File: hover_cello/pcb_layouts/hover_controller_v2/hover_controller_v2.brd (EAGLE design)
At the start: 101.6 x 50.8 mm, 33 parts, among them IC1 74LS279N, U1 L298

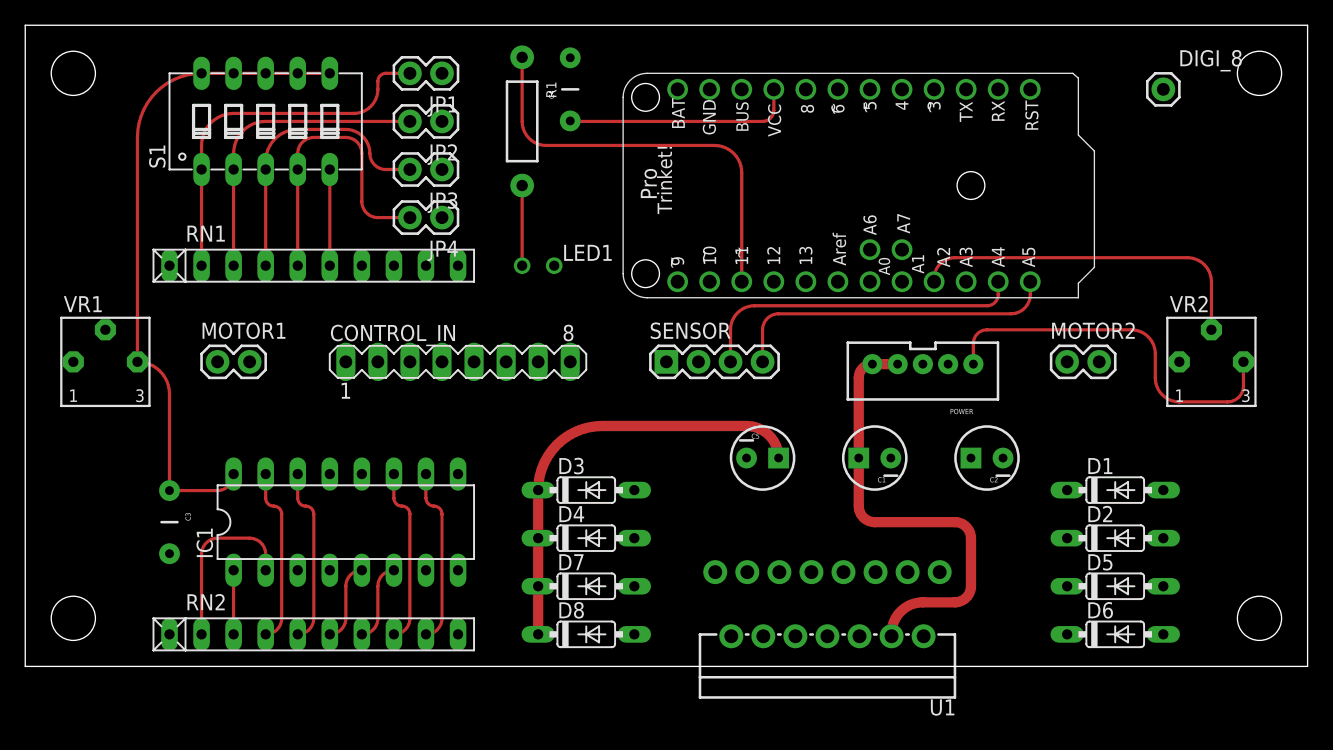
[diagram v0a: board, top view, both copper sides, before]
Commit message: wrote and tested V1.0 firmware for hover cello
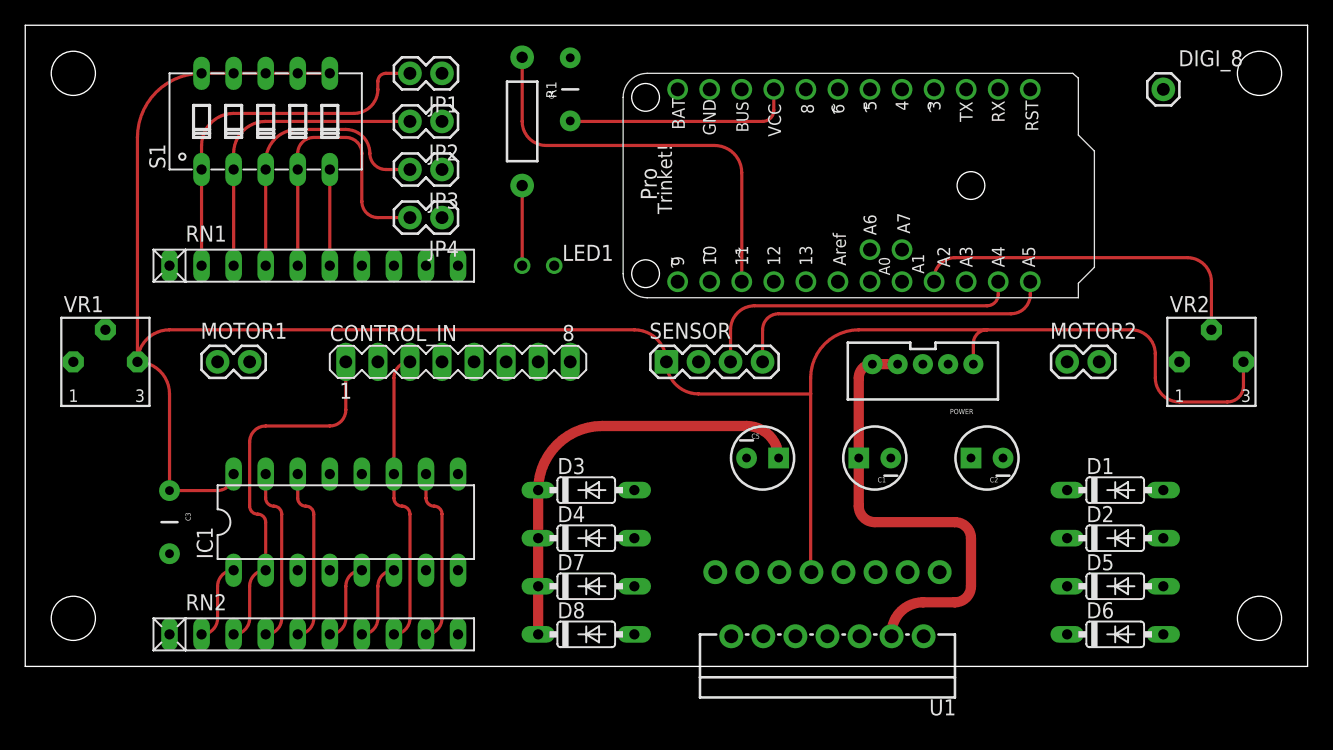
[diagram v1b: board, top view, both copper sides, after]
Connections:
- net R1: now also RN2.2; no longer RN2.3
- net S1: now also RN2.3; no longer RN2.2
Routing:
- net VCC: track 81.4 -> 168.9 mm
- net S1: track 13.8 -> 29.3 mm
- net S2: track 13.8 -> 23.2 mm
- net R1: track 5.08 -> 6.13 mm
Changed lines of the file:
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@@
 <contactref element="VR1" pad="3"/>
 <contactref element="VR2" pad="3"/>
-<wire x1="75.12" y1="23.95" x2="75.12" y2="25.59" width="0.254" layer="1"/>
-<wire x1="75.12" y1="25.59" x2="76.2" y2="26.67" width="0.254" layer="1" curve="-90"/>
+<wire x1="76.2" y1="26.67" x2="75.12" y2="25.59" width="0.254" layer="1" curve="90"/>
 <wire x1="87.63" y1="26.67" x2="89.535" y2="24.765" width="0.254" layer="1" curve="-90"/>
 <wire x1="89.535" y1="24.765" x2="89.535" y2="22.86" width="0.254" layer="1"/>
@@
 <wire x1="13.97" y1="46.99" x2="8.89" y2="41.91" width="0.254" layer="1" curve="90"/>
 <wire x1="8.89" y1="41.91" x2="8.89" y2="24.13" width="0.254" layer="1"/>
-<wire x1="74.93" y1="16.51" x2="75.12" y2="23.95" width="0" layer="19" extent="1-1"/>
-<wire x1="62.29" y1="7.47" x2="74.93" y2="16.51" width="0" layer="19" extent="1-1"/>
-<wire x1="50.8" y1="24.13" x2="62.29" y2="7.47" width="0" layer="19" extent="1-1"/>
-<wire x1="24.13" y1="46.99" x2="50.8" y2="24.13" width="0" layer="19" extent="1-1"/>
+<wire x1="75.12" y1="23.95" x2="75.12" y2="25.59" width="0.254" layer="1"/>
+<wire x1="62.29" y1="7.47" x2="62.23" y2="7.53" width="0.254" layer="1" curve="-90"/>
+<wire x1="62.23" y1="21.59" x2="62.23" y2="7.53" width="0.254" layer="1"/>
+<wire x1="62.23" y1="21.59" x2="62.23" y2="22.86" width="0.254" layer="1"/>
+<wire x1="62.23" y1="22.86" x2="66.04" y2="26.67" width="0.254" layer="1" curve="-90"/>
+<wire x1="66.04" y1="26.67" x2="76.2" y2="26.67" width="0.254" layer="1"/>
+<wire x1="53.34" y1="21.59" x2="50.8" y2="24.13" width="0.254" layer="1" curve="-90"/>
+<wire x1="53.34" y1="21.59" x2="62.23" y2="21.59" width="0.254" layer="1"/>
+<wire x1="50.8" y1="24.13" x2="48.26" y2="26.67" width="0.254" layer="1" curve="90"/>
+<wire x1="11.43" y1="26.67" x2="8.89" y2="24.13" width="0.254" layer="1" curve="90"/>
+<wire x1="48.26" y1="26.67" x2="11.43" y2="26.67" width="0.254" layer="1"/>
+<wire x1="75.12" y1="23.95" x2="74.93" y2="16.51" width="0" layer="19" extent="1-1"/>
 <wire x1="21.59" y1="46.99" x2="24.13" y2="46.99" width="0" layer="19" extent="1-1"/>
 <wire x1="19.05" y1="46.99" x2="21.59" y2="46.99" width="0" layer="19" extent="1-1"/>
@@
 <contactref element="CONTROL_IN" pad="1"/>
 <contactref element="IC1" pad="2"/>
-<contactref element="RN2" pad="2"/>
-<wire x1="13.97" y1="8.89" x2="15.24" y2="10.16" width="0.254" layer="1" curve="-90"/>
-<wire x1="15.24" y1="10.16" x2="17.78" y2="10.16" width="0.254" layer="1"/>
-<wire x1="17.78" y1="10.16" x2="19.05" y2="8.89" width="0.254" layer="1" curve="-90"/>
-<wire x1="19.05" y1="8.89" x2="19.05" y2="7.62" width="0.254" layer="1"/>
-<wire x1="13.97" y1="2.54" x2="13.97" y2="8.89" width="0.254" layer="1"/>
-<wire x1="17.78" y1="10.16" x2="25.4" y2="24.13" width="0" layer="19" extent="1-1"/>
+<contactref element="RN2" pad="3"/>
+<wire x1="16.51" y1="2.54" x2="17.78" y2="3.81" width="0.254" layer="1" curve="90"/>
+<wire x1="17.78" y1="3.81" x2="17.78" y2="6.35" width="0.254" layer="1"/>
+<wire x1="19.05" y1="7.62" x2="17.78" y2="6.35" width="0.254" layer="1" curve="90"/>
+<wire x1="25.4" y1="24.13" x2="25.4" y2="20.32" width="0.254" layer="1"/>
+<wire x1="25.4" y1="20.32" x2="24.13" y2="19.05" width="0.254" layer="1" curve="-90"/>
+<wire x1="24.13" y1="19.05" x2="19.05" y2="19.05" width="0.254" layer="1"/>
+<wire x1="19.05" y1="19.05" x2="17.78" y2="17.78" width="0.254" layer="1" curve="90"/>
+<wire x1="17.78" y1="17.78" x2="17.78" y2="12.7" width="0.254" layer="1"/>
+<wire x1="17.78" y1="12.7" x2="18.415" y2="12.065" width="0.254" layer="1" curve="90"/>
+<wire x1="18.415" y1="12.065" x2="19.05" y2="11.43" width="0.254" layer="1" curve="-90"/>
+<wire x1="19.05" y1="11.43" x2="19.05" y2="7.62" width="0.254" layer="1"/>
 </signal>
 <signal name="R1">
 <contactref element="CONTROL_IN" pad="2"/>
 <contactref element="IC1" pad="1"/>
-<contactref element="RN2" pad="3"/>
-<wire x1="16.51" y1="2.54" x2="16.51" y2="7.62" width="0.254" layer="1"/>
+<contactref element="RN2" pad="2"/>
+<wire x1="13.97" y1="2.54" x2="15.24" y2="3.81" width="0.254" layer="1" curve="90"/>
+<wire x1="15.24" y1="3.81" x2="15.24" y2="6.35" width="0.254" layer="1"/>
+<wire x1="15.24" y1="6.35" x2="16.51" y2="7.62" width="0.254" layer="1" curve="-90"/>
 <wire x1="16.51" y1="7.62" x2="27.94" y2="24.13" width="0" layer="19" extent="1-1"/>
 </signal>
@@
 <wire x1="30.48" y1="12.065" x2="29.845" y2="12.7" width="0.254" layer="1" curve="90"/>
 <wire x1="29.845" y1="12.7" x2="29.21" y2="13.335" width="0.254" layer="1" curve="-90"/>
-<wire x1="29.21" y1="13.335" x2="29.21" y2="15.24" width="0.254" layer="1"/>
+<wire x1="29.21" y1="15.24" x2="29.21" y2="13.335" width="0.254" layer="1"/>
 <wire x1="30.48" y1="3.81" x2="30.48" y2="12.065" width="0.254" layer="1"/>
-<wire x1="29.21" y1="15.24" x2="30.48" y2="24.13" width="0" layer="19" extent="1-1"/>
+<wire x1="30.48" y1="24.13" x2="29.21" y2="22.86" width="0.254" layer="1" curve="90"/>
+<wire x1="29.21" y1="22.86" x2="29.21" y2="15.24" width="0.254" layer="1"/>
 </signal>
 <signal name="R2">
@@
 <wire x1="33.02" y1="12.065" x2="32.385" y2="12.7" width="0.254" layer="1" curve="90"/>
 <wire x1="32.385" y1="12.7" x2="31.75" y2="13.335" width="0.254" layer="1" curve="-90"/>
-<wire x1="31.75" y1="13.335" x2="31.75" y2="15.24" width="0.254" layer="1"/>
+<wire x1="31.75" y1="15.24" x2="31.75" y2="13.335" width="0.254" layer="1"/>
 <wire x1="33.02" y1="3.81" x2="33.02" y2="12.065" width="0.254" layer="1"/>
 <wire x1="31.75" y1="15.24" x2="33.02" y2="24.13" width="0" layer="19" extent="1-1"/>
